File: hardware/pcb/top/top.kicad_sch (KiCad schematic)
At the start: 32 parts, among them J1 OLED_128x32, J2 Conn_01x15, SW1 SLW-864574-5A-RA-N-D, SW2 RotaryEncoder_Switch

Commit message: migrate kicad projects from v8 to v9
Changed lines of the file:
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@@
 (kicad_sch
-	(version 20231120)
+	(version 20250114)
 	(generator "eeschema")
-	(generator_version "8.0")
+	(generator_version "9.0")
 	(paper "A4")
+	(rectangle
+		(start 185.42 49.53)
+		(end 213.36 82.55)
+		(stroke
+			(width 0)
+			(type default)
+		)
+		(fill
+			(type none)
+		)
+	)
+	(rectangle
+		(start 133.35 49.53)
+		(end 184.15 137.16)
+		(stroke
+			(width 0)
+			(type default)
+		)
+		(fill
+			(type none)
+		)
+	)
+	(text "Switch Matrix"
+		(exclude_from_sim no)
+		(at 98.806 53.594 0)
+		(effects
+			(font
+				(size 2.54 2.54)
+				(thickness 0.508)
+				(bold yes)
+			)
+		)
+	)
+	(text "Main Board"
+		(exclude_from_sim no)
+		(at 198.12 88.9 0)
+		(effects
+			(font
+				(size 2.54 2.54)
+				(bold yes)
+			)
+		)
+	)
+	(text "Peripherics"
+		(exclude_from_sim no)
+		(at 157.734 53.594 0)
+		(effects
+			(font
+				(size 2.54 2.54)
+				(thickness 0.508)
+				(bold yes)
+			)
+		)
+	)
+	(text "Layout"
+		(exclude_from_sim no)
+		(at 199.39 53.34 0)
+		(effects
+			(font
+				(size 2.54 2.54)
+				(bold yes)
+			)
+		)
+	)
+	(text "SPDT Switch \nfor Mode Switching"
+		(exclude_from_sim no)
+		(at 160.02 88.9 0)
+		(effects
+			(font
+				(size 1.905 1.905)
+			)
+		)
+	)
+	(text "EC11 Rotary Encoder\nwith push button"
+		(exclude_from_sim no)
+		(at 160.02 115.57 0)
+		(effects
+			(font
+				(size 1.905 1.905)
+			)
+		)
+	)
+	(text "SSD1306 128 x 32\nOLED Display"
+		(exclude_from_sim no)
+		(at 157.48 60.96 0)
+		(effects
+			(font
+				(size 1.905 1.905)
+			)
+		)
+	)
+	(text "Top Board"
+		(exclude_from_sim no)
+		(at 215.392 173.736 0)
+		(effects
+			(font
+				(size 5.08 5.08)
+				(thickness 1.016)
+				(bold yes)
+			)
+		)
+	)
 	(junction
 		(at 107.95 60.96)
@@
 		)
 	)
-	(rectangle
-		(start 185.42 49.53)
-		(end 213.36 82.55)
-		(stroke
-			(width 0)
-			(type default)
-		)
-		(fill
-			(type none)
-		)
-	)
-	(rectangle
-		(start 133.35 49.53)
-		(end 184.15 137.16)
-		(stroke
-			(width 0)
-			(type default)
-		)
-		(fill
-			(type none)
-		)
-	)
-	(text "Switch Matrix"
-		(exclude_from_sim no)
-		(at 98.806 53.594 0)
-		(effects
-			(font
-				(size 2.54 2.54)
-				(thickness 0.508)
-				(bold yes)
-			)
-		)
-	)
-	(text "Main Board"
-		(exclude_from_sim no)
-		(at 198.12 88.9 0)
-		(effects
-			(font
-				(size 2.54 2.54)
-				(bold yes)
-			)
-		)
-	)
-	(text "Peripherics"
-		(exclude_from_sim no)
-		(at 157.734 53.594 0)
-		(effects
-			(font
-				(size 2.54 2.54)
-				(thickness 0.508)
-				(bold yes)
-			)
-		)
-	)
-	(text "Layout"
-		(exclude_from_sim no)
-		(at 199.39 53.34 0)
-		(effects
-			(font
-				(size 2.54 2.54)
-				(bold yes)
-			)
-		)
-	)
-	(text "SPDT Switch \nfor Mode Switching"
-		(exclude_from_sim no)
-		(at 160.02 88.9 0)
-		(effects
-			(font
-				(size 1.905 1.905)
-			)
-		)
-	)
-	(text "EC11 Rotary Encoder\nwith push button"
-		(exclude_from_sim no)
-		(at 160.02 115.57 0)
-		(effects
-			(font
-				(size 1.905 1.905)
-			)
-		)
-	)
-	(text "SSD1306 128 x 32\nOLED Display"
-		(exclude_from_sim no)
-		(at 157.48 60.96 0)
-		(effects
-			(font
-				(size 1.905 1.905)
-			)
-		)
-	)
-	(text "Top Board"
-		(exclude_from_sim no)
-		(at 215.392 173.736 0)
-		(effects
-			(font
-				(size 5.08 5.08)
-				(thickness 1.016)
-				(bold yes)
-			)
-		)
-	)
 	(global_label "ROW0"
 		(shape input)
@@
 		(at 190.5 59.69 0)
 		(unit 1)
-		(exclude_from_sim yes)
+		(exclude_from_sim no)
 		(in_bom no)
 		(on_board yes)
@@
 		(at 205.74 72.39 0)
 		(unit 1)
-		(exclude_from_sim yes)
+		(exclude_from_sim no)
 		(in_bom no)
 		(on_board yes)
@@
 		(at 190.5 72.39 0)
 		(unit 1)
-		(exclude_from_sim yes)
+		(exclude_from_sim no)
 		(in_bom no)
 		(on_board yes)
@@
 		(at 205.74 59.69 0)
 		(unit 1)
-		(exclude_from_sim yes)
+		(exclude_from_sim no)
 		(in_bom no)
 		(on_board yes)
@@
 		)
 	)
+	(embedded_fonts no)
 )

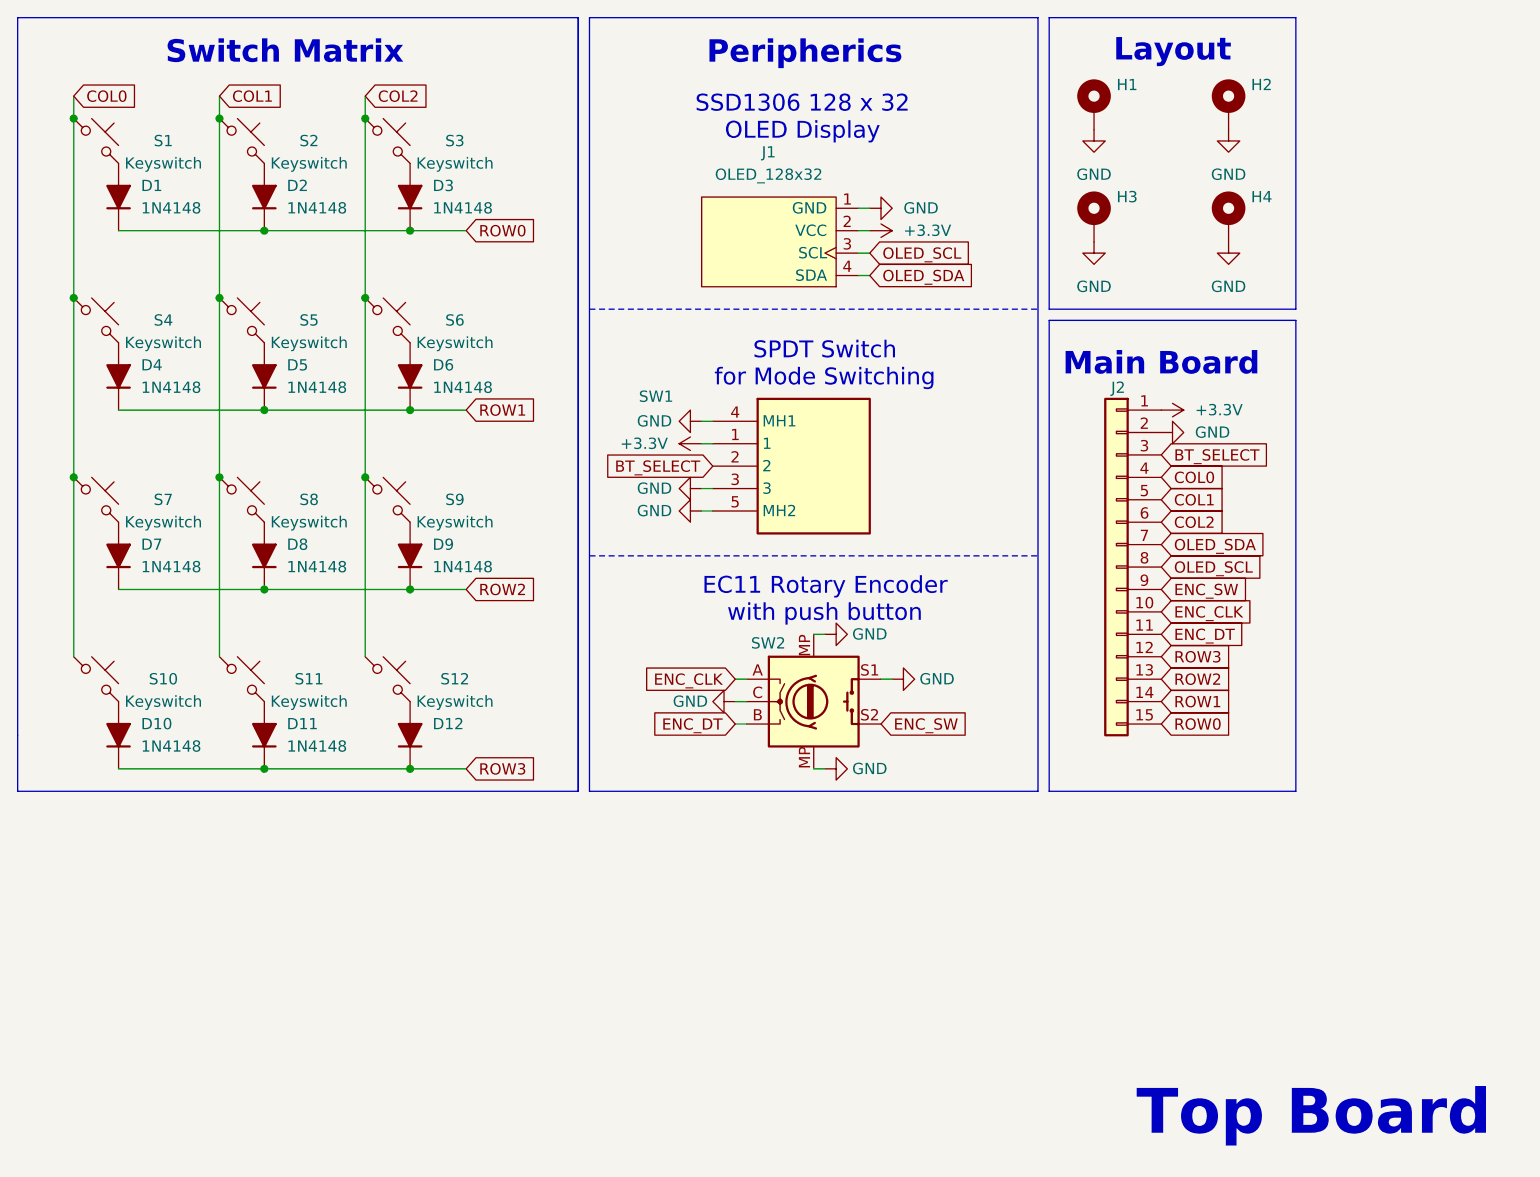
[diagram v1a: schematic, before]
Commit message: update documentation images, remove copper pours and vias from top plate, minor fixes
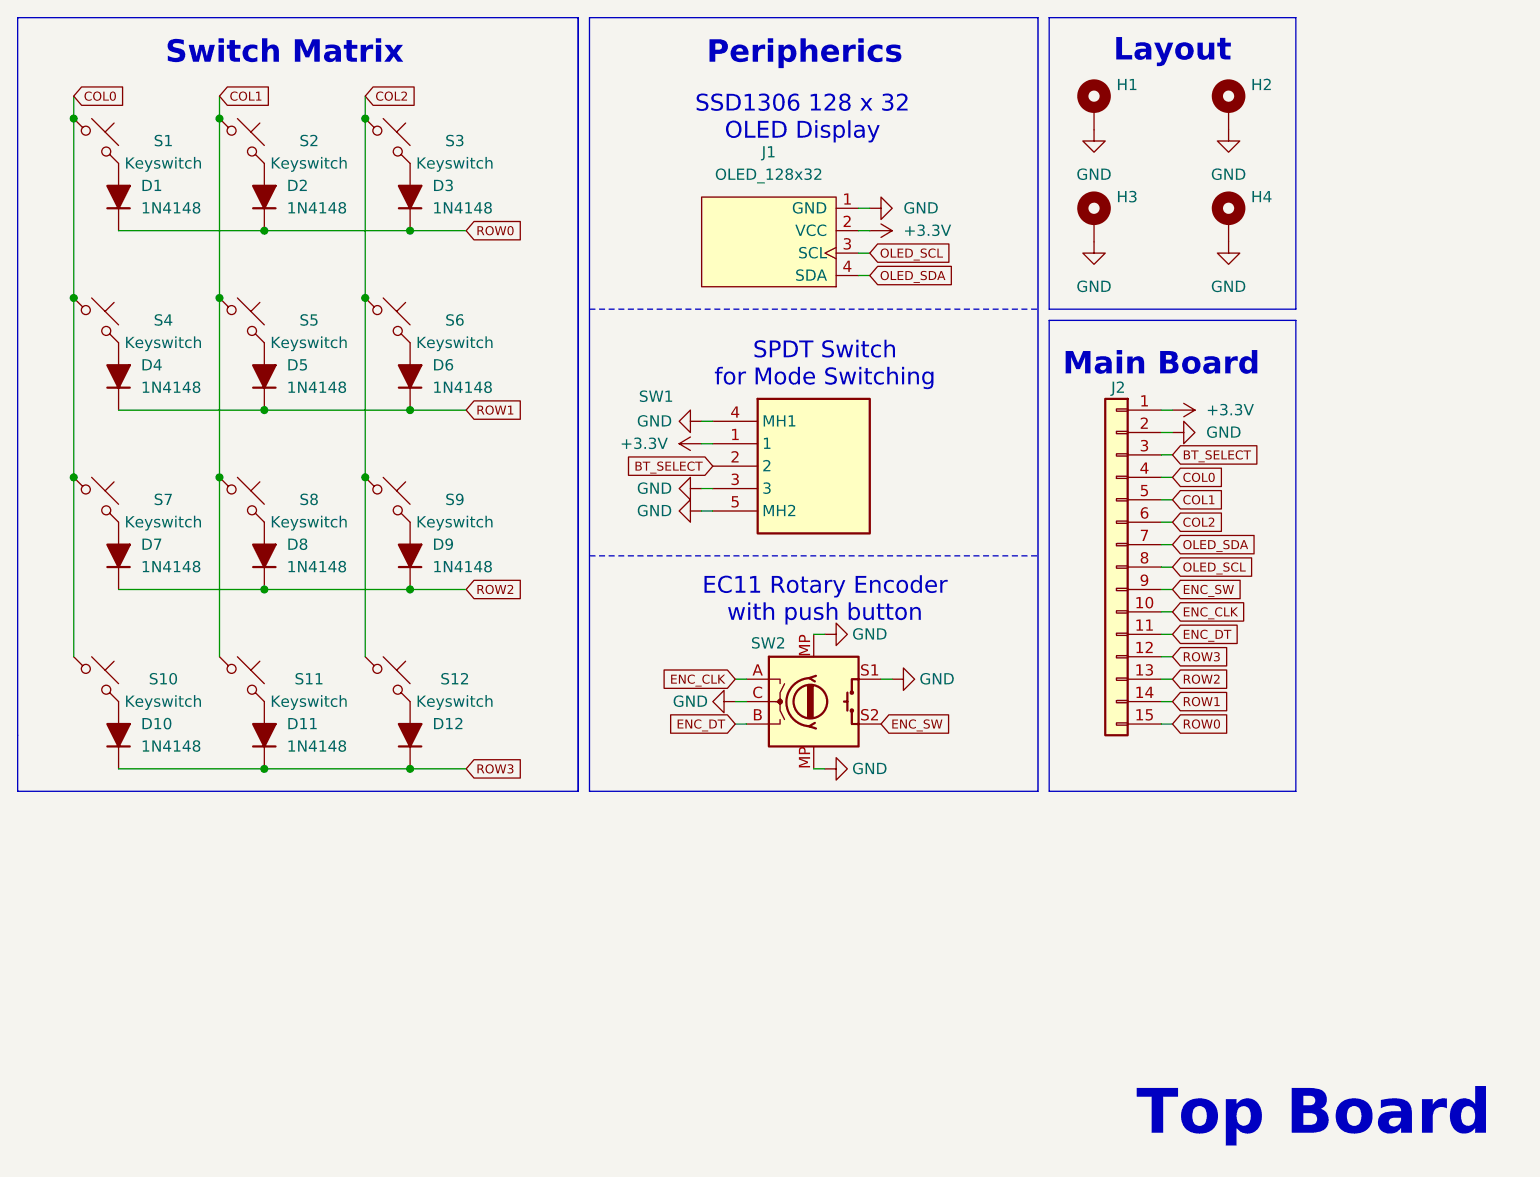
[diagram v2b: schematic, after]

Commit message: changed m2.5 mh to m2, added screws and nuts to enclosure.FCStd
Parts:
- removed SW2: RotaryEncoder_Switch, Top-Footprints:Encoder_EC11_MX, symbol Top-Symbols:RotaryEncoder_Switch
- added SW2: RotaryEncoder_Switch, Top-Footprints:Encoder_EC11_MX, symbol Device:RotaryEncoder_Switch
- H1, H2, H3, H4: footprint Top-Footprints:MountingHole_2.5mm_Pad -> MountingHole:MountingHole_2.2mm_M2_DIN965_Pad
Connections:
- net ENC_CLK: now also SW2.A
- net ENC_DT: now also SW2.B
- net ENC_SW: now also SW2.S2
- net GND: now also SW2.C, SW2.S1
